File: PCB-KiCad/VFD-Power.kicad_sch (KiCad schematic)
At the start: 23 parts, among them IC1 74132D, IC2 XL6009, IC3 ZXBM5210, U3 R-78B5.0-2.0

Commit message: Fixed merge issues.
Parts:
- removed C4, C8: 1u, VFD-Power:C1206, symbol VFD-Power-eagle-import:CPOL-EU153CLV-0505
- added C10, C4: 1u, Capacitor_SMD:C_0603_1608Metric_Pad1.08x0.95mm_HandSolder, symbol Device:C_Polarized_Small
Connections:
- net GND: now also C10.2, C4.2
- net VPP: now also C10.1
- net at IC3.2 (VM), L1.2, L2.2: now also C4.1
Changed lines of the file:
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@@
-    (stroke (width 0) (type default))
-  )
-  (wire (pts (xy 112.522 151.384) (xy 112.522 147.32))
     (stroke (width 0) (type default))
   )
@@
     (stroke (width 0.1524) (type solid))
   )
+  (wire (pts (xy 189.23 64.77) (xy 189.23 71.12))
+    (stroke (width 0.1524) (type solid))
+  )
   (wire (pts (xy 179.07 45.72) (xy 179.07 53.34))
     (stroke (width 0.1524) (type solid))
@@
     (stroke (width 0.1524) (type solid))
   )
-  (wire (pts (xy 189.23 71.12) (xy 189.23 67.31))
-    (stroke (width 0.1524) (type solid))
-  )
   (wire (pts (xy 29.21 172.72) (xy 29.21 154.94))
     (stroke (width 0.1524) (type solid))
@@
   (wire (pts (xy 69.85 50.8) (xy 63.5 50.8))
     (stroke (width 0.1524) (type solid))
+  )
+  (wire (pts (xy 112.522 147.32) (xy 112.522 153.924))
+    (stroke (width 0) (type default))
   )
   (wire (pts (xy 130.81 53.34) (xy 137.16 53.34))
@@
         (path "/d66e9896-ee3f-419d-ab82-78a854ae4100"
           (reference "IC3") (unit 1)
-        )
-      )
-    )
-  )
-  (symbol (lib_id "VFD-Power-eagle-import:CPOL-EU153CLV-0505") (at 112.522 153.924 0) (unit 1)
-    (in_bom yes) (on_board yes) (dnp no)
-    (property "Reference" "C4" (at 113.665 153.4414 0)
-      (effects (font (size 1.778 1.5113)) (justify left bottom))
-    )
-    (property "Value" "1u" (at 113.665 158.5214 0)
-      (effects (font (size 1.778 1.5113)) (justify left bottom))
-    )
-    (property "Footprint" "VFD-Power:C1206" (at 112.522 153.924 0)
-      (effects (font (size 1.27 1.27)) hide)
-    )
-    (property "Datasheet" "" (at 112.522 153.924 0)
-      (effects (font (size 1.27 1.27)) hide)
-    )
-    (pin "+")
-    (pin "-")
-    (instances
-      (project "GP1294-Teens4"
-        (path "/3de011e3-f89b-42a8-8637-1f4c3f0867fa/9e049bd2-8c7e-4a7a-b856-b0fbd11ae8df"
-          (reference "C4") (unit 1)
-        )
-      )
-      (project "VFD-Power"
-        (path "/d66e9896-ee3f-419d-ab82-78a854ae4100"
-          (reference "C4") (unit 1)
         )
       )
@@
     )
   )
+  (symbol (lib_id "Device:C_Polarized_Small") (at 189.23 62.23 0) (unit 1)
+    (in_bom yes) (on_board yes) (dnp no) (fields_autoplaced)
+    (property "Reference" "C4" (at 192.024 60.4139 0)
+      (effects (font (size 1.27 1.27)) (justify left))
+    )
+    (property "Value" "1u" (at 192.024 62.9539 0)
+      (effects (font (size 1.27 1.27)) (justify left))
+    )
+    (property "Footprint" "Capacitor_SMD:C_0603_1608Metric_Pad1.08x0.95mm_HandSolder" (at 189.23 62.23 0)
+      (effects (font (size 1.27 1.27)) hide)
+    )
+    (property "Datasheet" "~" (at 189.23 62.23 0)
+      (effects (font (size 1.27 1.27)) hide)
+    )
+    (pin "1")
+    (pin "2")
+    (instances
+      (project "GP1294-Teens4"
+        (path "/3de011e3-f89b-42a8-8637-1f4c3f0867fa/9e049bd2-8c7e-4a7a-b856-b0fbd11ae8df"
+          (reference "C4") (unit 1)
+        )
+      )
+    )
+  )
   (symbol (lib_id "VFD-Power-eagle-import:C-EUC1206") (at 105.41 154.94 0) (unit 1)
     (in_bom yes) (on_board yes) (dnp no)
@@
     )
   )
-  (symbol (lib_id "VFD-Power-eagle-import:CPOL-EU153CLV-0505") (at 189.23 62.23 0) (unit 1)
-    (in_bom yes) (on_board yes) (dnp no)
-    (property "Reference" "C8" (at 190.373 61.7474 0)
-      (effects (font (size 1.778 1.5113)) (justify left bottom))
-    )
-    (property "Value" "1u" (at 190.373 66.8274 0)
-      (effects (font (size 1.778 1.5113)) (justify left bottom))
-    )
-    (property "Footprint" "VFD-Power:C1206" (at 189.23 62.23 0)
-      (effects (font (size 1.27 1.27)) hide)
-    )
-    (property "Datasheet" "" (at 189.23 62.23 0)
-      (effects (font (size 1.27 1.27)) hide)
-    )
-    (pin "+")
-    (pin "-")
-    (instances
-      (project "GP1294-Teens4"
-        (path "/3de011e3-f89b-42a8-8637-1f4c3f0867fa/9e049bd2-8c7e-4a7a-b856-b0fbd11ae8df"
-          (reference "C8") (unit 1)
-        )
-      )
-      (project "VFD-Power"
-        (path "/d66e9896-ee3f-419d-ab82-78a854ae4100"
-          (reference "C8") (unit 1)
-        )
-      )
-    )
-  )
   (symbol (lib_id "VFD-Power-eagle-import:74132D") (at 229.87 93.98 0) (unit 2)
     (in_bom yes) (on_board yes) (dnp no)
@@
         )
       )
+    )
+  )
+  (symbol (lib_id "Device:C_Polarized_Small") (at 112.522 156.464 0) (unit 1)
+    (in_bom yes) (on_board yes) (dnp no) (fields_autoplaced)
+    (property "Reference" "C10" (at 115.316 154.6479 0)
+      (effects (font (size 1.27 1.27)) (justify left))
+    )
+    (property "Value" "1u" (at 115.316 157.1879 0)
+      (effects (font (size 1.27 1.27)) (justify left))
+    )
+    (property "Footprint" "Capacitor_SMD:C_0603_1608Metric_Pad1.08x0.95mm_HandSolder" (at 112.522 156.464 0)
+      (effects (font (size 1.27 1.27)) hide)
+    )
+    (property "Datasheet" "~" (at 112.522 156.464 0)
+      (effects (font (size 1.27 1.27)) hide)
+    )
+    (pin "1")
+    (pin "2")
+    (instances
+      (project "GP1294-Teens4"
+        (path "/3de011e3-f89b-42a8-8637-1f4c3f0867fa/9e049bd2-8c7e-4a7a-b856-b0fbd11ae8df"
+          (reference "C10") (unit 1)
+        )
+      )

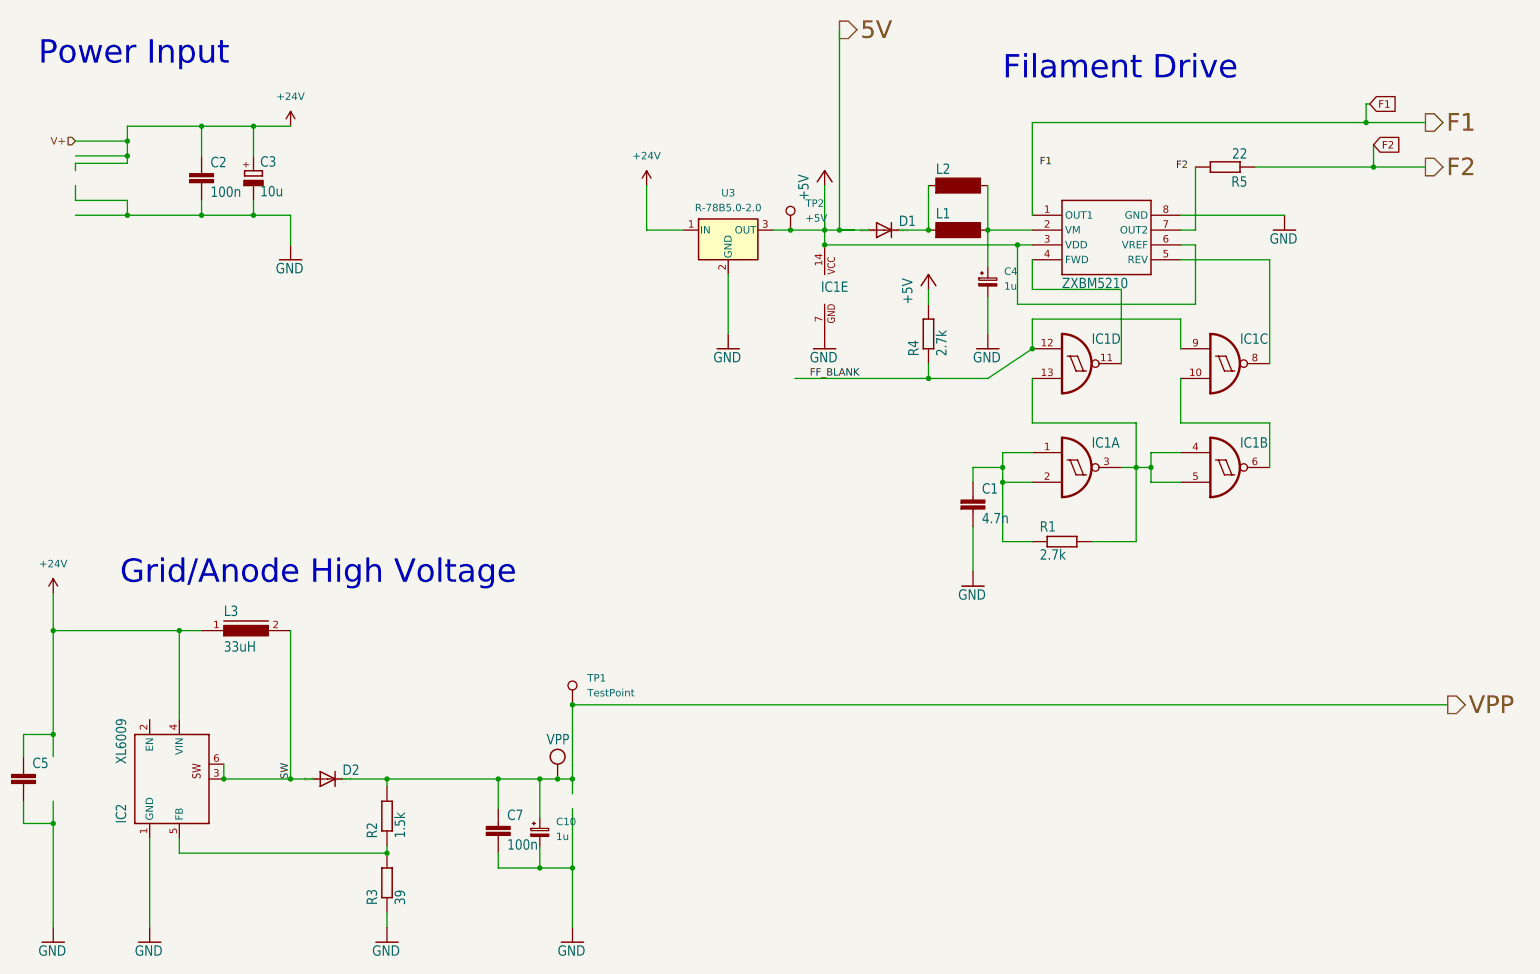
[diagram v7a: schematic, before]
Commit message: Upgraded Power circuit.
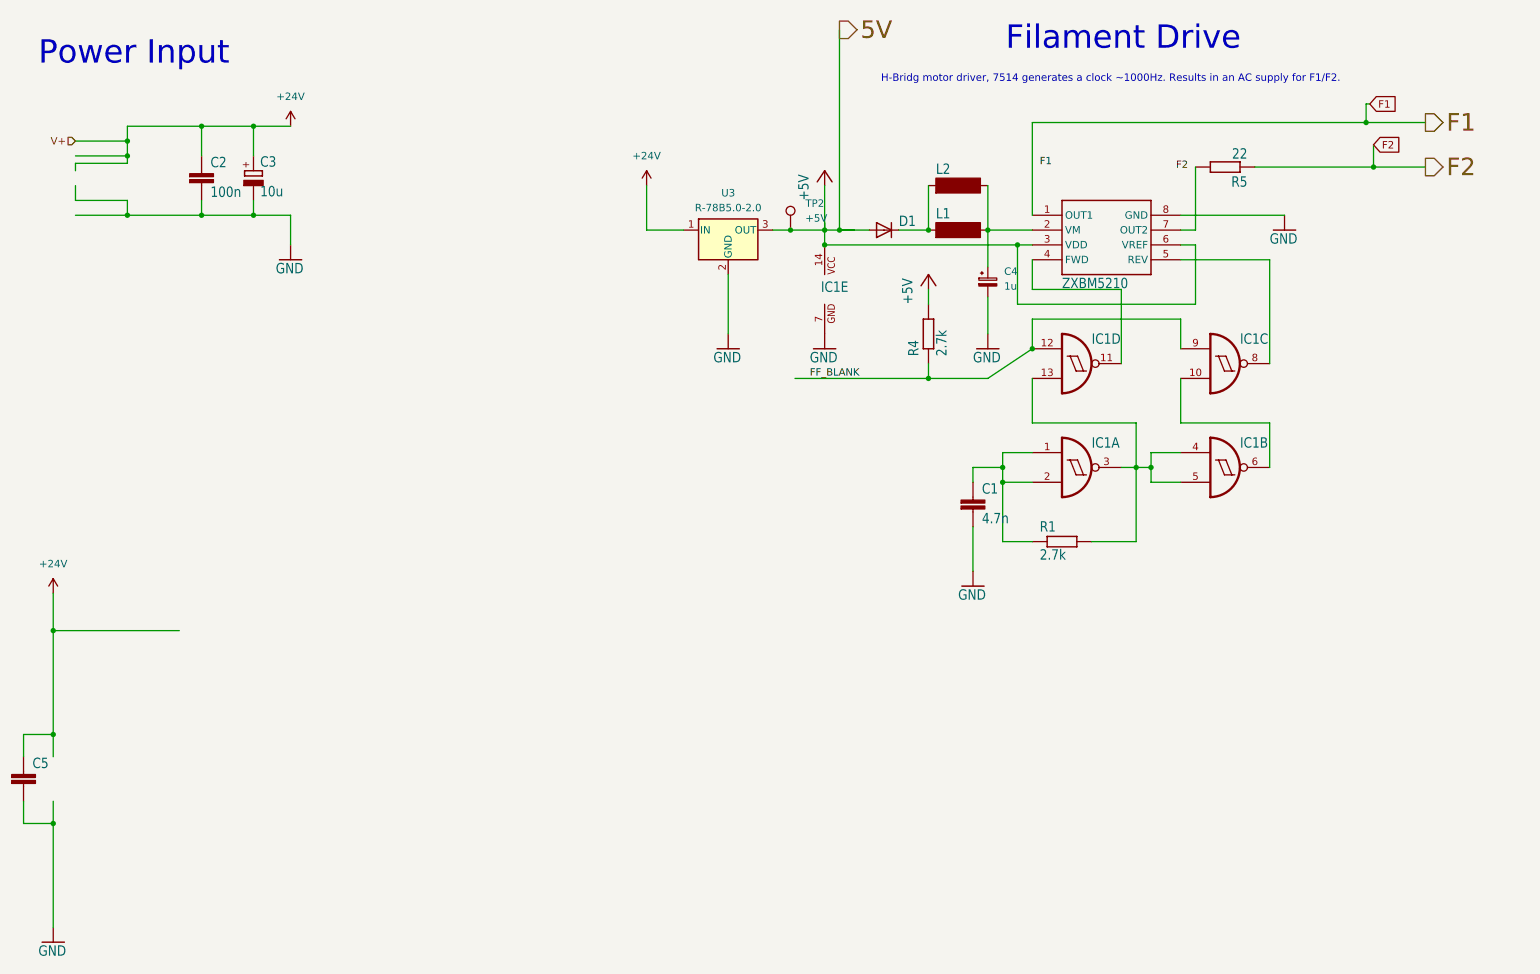
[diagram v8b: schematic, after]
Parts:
- removed C10: 1u, Capacitor_SMD:C_0603_1608Metric_Pad1.08x0.95mm_HandSolder, symbol Device:C_Polarized_Small
- removed C7: 100n, VFD-Power:C1206, symbol VFD-Power-eagle-import:C-EUC1206
- removed D2: SW-SMB, VFD-Power:SMB, symbol VFD-Power-eagle-import:DIODE-SMB
- removed IC2: XL6009, VFD-Power:TO263-5, symbol VFD-Power-eagle-import:XL6009
- removed L3: 33uH, VFD-Power:DR125, symbol VFD-Power-eagle-import:DR125
- removed R2: 1.5k, VFD-Power:R1206, symbol VFD-Power-eagle-import:R-EU_R1206
- removed R3: 39, VFD-Power:R1206, symbol VFD-Power-eagle-import:R-EU_R1206
- removed TP1: TestPoint, TestPoint:TestPoint_Pad_2.0x2.0mm, symbol Connector:TestPoint
- D1: footprint VFD-Power:SMB -> Diode_SMD:Nexperia_CFP3_SOD-123W; symbol VFD-Power-eagle-import:DIODE-SMB -> VFD-Power:DIODE-SOD123
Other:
- note added: "H-Bridg motor driver, 7514 generates a clock ~1000Hz. Results in an AC supply for F1/F2."
- note removed: "Grid/Anode High Voltage"
